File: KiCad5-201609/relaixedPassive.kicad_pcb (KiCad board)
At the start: 2 copper layers, 83 x 74 mm, 68 parts, among them IC1 SN74HC595NSR, IC2 SN74HC595NSR, J1 TFM-105-01-F-D, K1 RELAY_G6K_AB, K10 RELAY_G6K, K11 RELAY_G6K, K12 RELAY_G6K, K13 RELAY_G6K, K14 RELAY_G6K, K2 CINCH-DUAL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

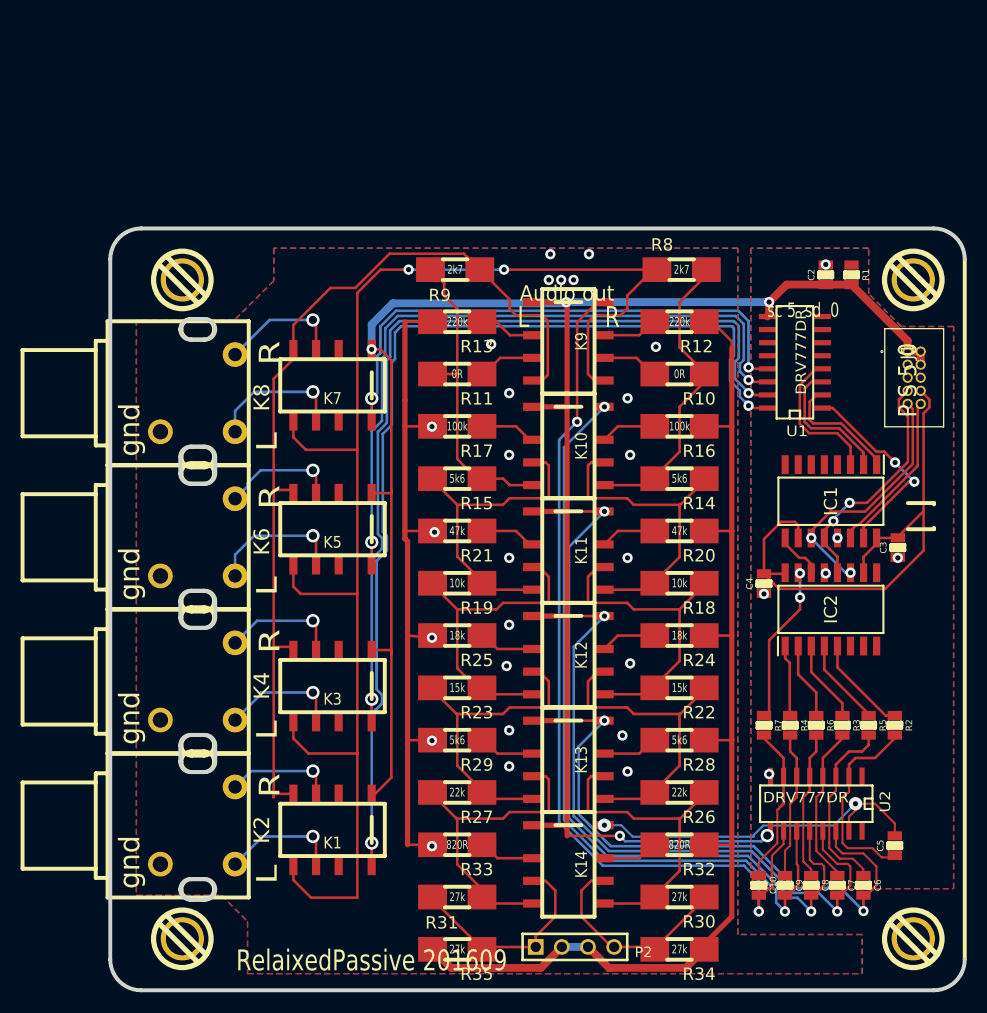
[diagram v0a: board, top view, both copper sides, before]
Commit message: moved control to side, added electrolytic caps
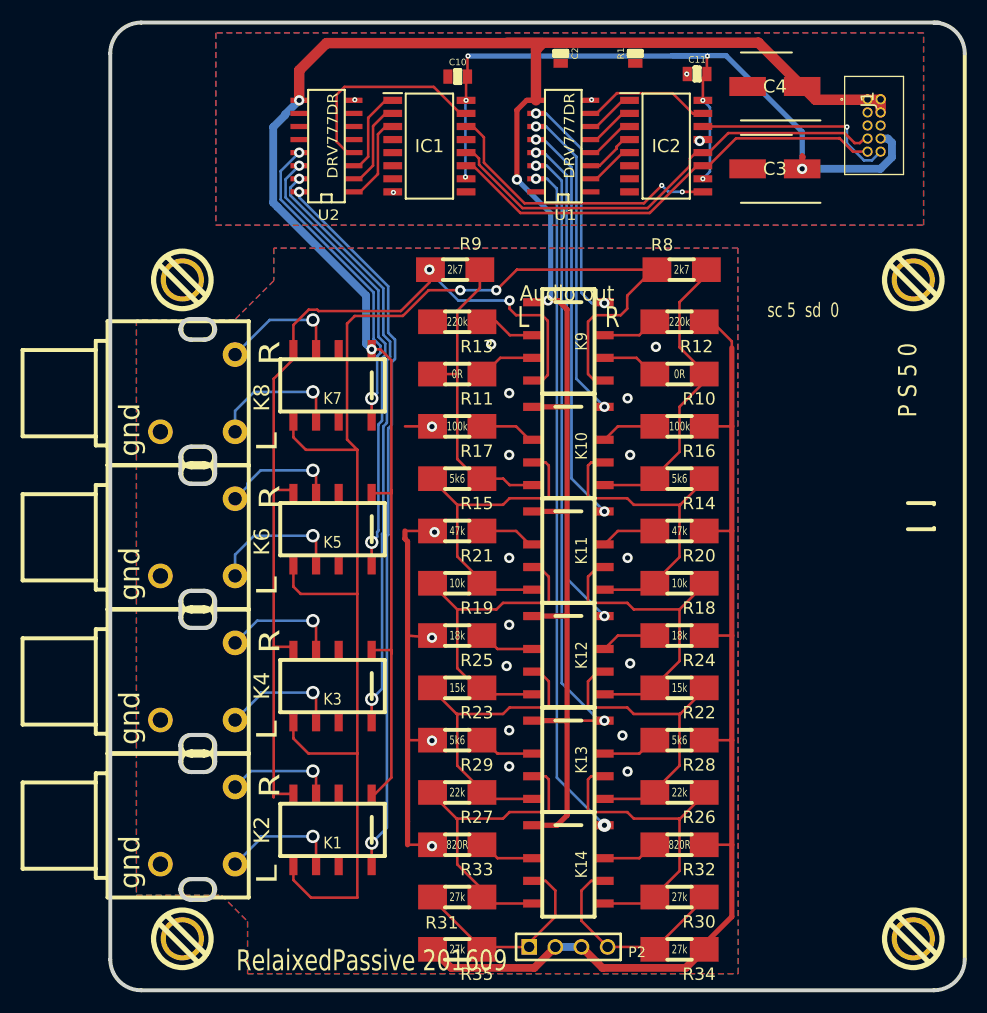
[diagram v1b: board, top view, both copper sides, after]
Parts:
- removed the C10 at (103.0, 103.8)
- removed C5, C6, C7, C8, C9: 470nF, RlxPassiveFootprints:R0805
- removed R2, R3, R4, R5, R6, R7: 4k7, RlxPassiveFootprints:R0805
- added C3: VZL221M1CTR-0607, Samacsys:CAPAE660X800N, F.Cu at (104.6, 34.2)
- added C4: VZL221M1CTR-0607, Samacsys:CAPAE660X800N, F.Cu at (104.6, 26.2)
- moved U1 68.4 mm to (84.0, 32.0), turned to 90 degrees
- moved C10 62.6 mm to (73.8, 25.2), turned to 0 degrees
- moved IC1 52.1 mm to (71.0, 32.0), turned to 0 degrees
- moved U2 50.1 mm to (61.0, 32.0)
- moved C11 49.9 mm to (97.0, 25.0), turned to 0 degrees
- moved IC2 47.8 mm to (94.0, 32.0), turned to 0 degrees
- moved C2 33.5 mm to (83.8, 23.0), turned to -90 degrees
- moved R1 30.1 mm to (91.0, 23.0), turned to 90 degrees
- moved J1 24.8 mm to (113.6, 27.5)
- moved P2 0.64 mm to (84.5, 109.8)
- turned R9 to 180 degrees
- renumbered C3 to C10, C4 to C11, U2 to U1, U1 to U2
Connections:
- IC1 pad 14: SER1 -> Net-(IC1-SER)
- IC1 pad 9: Net-(IC1-QH') -> unconnected-(IC1-QH'-Pad9)
- IC2 pad 14: Net-(IC1-QH') -> SER1
- IC2 pad 9: unconnected-(IC2-QH'-Pad9) -> Net-(IC1-SER)
- U1 pad 2: Net-(U2-I2) -> VL5c
- U1 pad 3: Net-(U2-I3) -> VL4c
- U1 pad 4: Net-(U2-I4) -> VL3c
- U1 pad 5: Net-(U2-I5) -> VL2c
- U1 pad 6: Net-(U2-I6) -> VL1c
- U1 pad 7: Net-(U2-I7) -> VL0c
- U2 pad 1: contCH1 -> contCH4
- U2 pad 2: contCH2 -> contCH3
- U2 pad 3: contCH3 -> contCH2
- U2 pad 4: contCH4 -> contCH1
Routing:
- net VL0: track 87.1 -> 23.3 mm
- net VL1: track 76.2 -> 30.6 mm
- net +5V: track 206.3 -> 245.3 mm, vias 5 -> 4
- net VL5: track 34.7 -> 66.2 mm
- net VL2: track 70.4 -> 39.3 mm
- net Net-(IC1-SER): track 0.00 -> 28.7 mm, vias 0 -> 2
- net CH1: track 97.4 -> 70.3 mm
- net +3.3V: track 54.8 -> 80.6 mm, vias 0 -> 7
- net CH2: track 82.7 -> 57.9 mm
- net CH3: track 67.1 -> 43.9 mm
- net AGND: track 173.8 -> 151.1 mm, vias 25 -> 20
- net RCLK1: track 23.9 -> 45.6 mm, vias 2 -> 0
- net CH4: track 52.8 -> 31.2 mm
- net SRCLK1: track 24.5 -> 44.5 mm, vias 2 -> 0
- net Net-(U2-I2): track 19.5 -> 0.00 mm
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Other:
- board size 83 x 74 mm -> 83 x 94 mm

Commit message: added output rca option
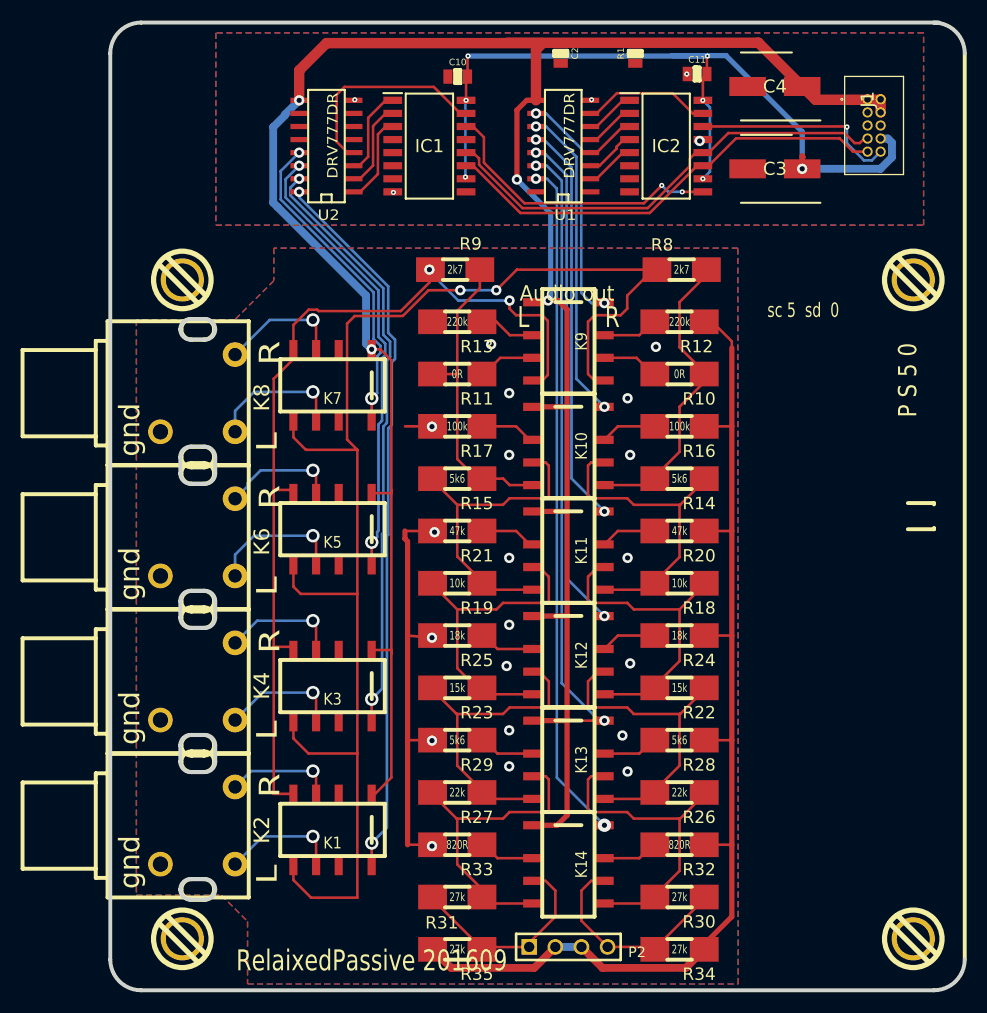
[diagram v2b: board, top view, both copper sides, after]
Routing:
- net Net-(K1-Pad4): track 90.6 -> 90.0 mm
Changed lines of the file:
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@@
 		(tags "CMS SOJ")
 		(property "Reference" "U1"
-			(at -6.69798 0.21082 360)
+			(at -6.69798 0.21082 0)
 			(layer "F.SilkS")
 			(effects
@@
 	)
 	(segment
-		(start 54.60492 99.05492)
+		(start 54.81828 99.05492)
 		(end 59.68492 99.05492)
 		(width 0.254)
@@
 	)
 	(segment
-		(start 54.60492 99.26828)
-		(end 52.12334 101.74986)
-		(width 0.254)
-		(layer "B.Cu")
-		(net 37)
-	)
-	(segment
-		(start 54.60492 99.05492)
-		(end 54.60492 99.26828)
+		(start 52.12334 101.74986)
+		(end 54.81828 99.05492)
 		(width 0.254)
 		(layer "B.Cu")
@@
 	)
 	(segment
-		(start 55.87492 94.9198)
-		(end 55.87492 95.24492)
-		(width 0.254)
-		(layer "F.Cu")
-		(net 86)
-	)
-	(segment
 		(start 82.5 48.96842)
 		(end 81.96 48.42842)
@@
 	)
 	(segment
+		(start 55.87492 80.63992)
+		(end 55.87492 94.9198)
+		(width 0.254)
+		(layer "F.Cu")
+		(net 86)
+	)
+	(segment
 		(start 57.4802 65.39992)
 		(end 57.79008 65.7098)
@@
 	)
 	(segment
-		(start 55.87492 80.63992)
-		(end 55.87492 95.24492)
-		(width 0.254)
-		(layer "F.Cu")
-		(net 86)
-	)
-	(segment
 		(start 82.5 54.23842)
 		(end 82.5 48.96842)
@@
 		(polygon
 			(pts
-				(xy 101 112.38992) (xy 100.95992 41.90492) (xy 55.88 41.91) (xy 55.88 45.085) (xy 52.07 48.895)
-				(xy 42.53992 48.88992) (xy 42.53992 104.76992) (xy 50.79492 104.76992) (xy 53.33492 107.30992) (xy 53.33492 112.38992)
+				(xy 101 113.38992) (xy 100.95992 41.90492) (xy 55.88 41.91) (xy 55.88 45.085) (xy 52.07 48.895)
+				(xy 42.53992 48.88992) (xy 42.53992 104.76992) (xy 50.79492 104.76992) (xy 53.33492 107.30992) (xy 53.33492 113.38992)
 			)
 		)
